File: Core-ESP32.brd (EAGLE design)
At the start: 149.8 x 80.5 mm, 58 parts, among them J2 CONNECTOR-GROVE-4P-2.0-347013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, Q1 BSS138, Q10 BSS138, Q11 BSS138, Q12 BSS138, Q13 BSS138, Q2 BSS138, Q3 BSS138, Q4 BSS138, Q5 BSS138, Q6 BSS138, Q7 BSS138, Q8 BSS138, Q9 BSS138

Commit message: 2.0
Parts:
- removed C4: 10uF, SPCoast:0805-CAP
- removed ESP32: ESP32, SPCoast:ESP32-LOLIN-OLED
- removed JP3: (no value), SparkFun-Connectors:1X06_LOCK
- added I2CLED32, I2CLED64: (no value), SPCoast:1X04_LOCK
- added IO-A, IO-B, IO-C: (no value), SparkFun-Connectors:1X06_LOCK
- added J5: (no value), SPCoast:RJ25-INVERTED
- added R27: 10k, SPCoast:0805-RES
- added U$1: ESP32-GEEKCREITDOITV1, SPCoast:ESP32-GEEKCREIT
- C2: value 150uF -> 1.0uF; device SPCoast:0810-CAP -> SPCoast:0805-CAP
- C3: value 1.0uF -> 10uF
- J1: device SPCoast:DCJ0202 -> SPCoast:RJ25-INVERTED
- J2: value CONNECTOR-GROVE-4P-2.0-3470130P1 -> (none); device SPCoast:4P-2.0 -> SPCoast:DCJ0202
- J3: value (none) -> CONNECTOR-GROVE-4P-2.0-3470130P1; device SPCoast:RJ25-INVERTED -> SPCoast:4P-2.0
- JP1: value 5v I2C Power -> LED
- JP2: value (none) -> 5v I2C Power; device SparkFun-Connectors:1X06_LOCK -> SparkFun-Connectors:1X02_LOCK
- R1: value 10k -> 220R
- VR5.0: value 5v -> 78M05B
- moved J2 127.0 mm to (17.8, 11.4), turned to 0 degrees
- moved JP2 112.2 mm to (143.5, 29.2), turned to 180 degrees
- moved J3 106.0 mm to (142.2, 36.8), turned to 90 degrees
- moved JP1 71.2 mm to (85.1, 69.8)
- moved R1 59.5 mm to (85.1, 64.8), turned to 270 degrees
- moved R2 45.7 mm to (41.9, 35.6), turned to 180 degrees
- moved R15 44.6 mm to (41.9, 43.2)
- moved Q1 43.1 mm to (102.9, 38.7), turned to 0 degrees
- moved Q2 41.0 mm to (41.9, 39.4), turned to 0 degrees
- moved R4 34.6 mm to (52.1, 35.6), turned to 180 degrees
- moved J1 31.6 mm to (40.6, 9.78)
- moved R3 31.4 mm to (47.0, 35.6), turned to 180 degrees
- moved VR5.0 22.2 mm to (15.2, 41.9)
- moved OSHW1 22.2 mm to (15.2, 52.1)
- moved R13 21.9 mm to (97.8, 35.6)
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- renumbered LED1 to MATRIX1, LED2 to MATRIX2
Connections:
- removed net D15H: J3.3, JP2.3, Q4.3, R17.1
- removed net D26H: J4.5, JP3.5, Q10.3, R23.1
- removed net D36: ESP32.GPIO36, Q8.2, R10.1
- removed net D36H: J4.3, JP3.3, Q8.3, R21.1
- removed net RXH: J3.4, JP2.4, Q5.3, R18.1
- removed net TXH: J3.5, JP2.5, Q6.3, R19.1
- new net D18: Q6.2, R6.1, U$1.IO18
- new net D18H: IO-C.2, J5.2, Q6.3, R19.1
- new net D19: Q7.2, R7.1, U$1.IO19
- new net D19H: IO-C.3, J5.3, Q7.3, R20.1
- new net D23: Q10.2, R10.1, U$1.IO23
- new net D23H: IO-C.4, J5.4, Q10.3, R23.1
- new net D27: U$1.IO27
- new net D32: U$1.IO32
- new net D33: U$1.IO33
- new net D4: Q4.2, R4.1, U$1.IO4
- new net D4H: IO-B.4, J4.4, Q4.3, R17.1
- new net D5: Q5.2, R5.1, U$1.IO5
- new net D5H: IO-B.5, J4.5, Q5.3, R18.1
- new net N$1: JP1.1, R1.1
- new net RX2: IO-A.5, J1.5, U$1.RX2
- new net TX2: IO-A.4, J1.4, U$1.TX2
- net +3V3: now also I2CLED32.3, I2CLED64.3, IO-A.1, J1.1, R2.2, R4.2, U$1.3V3; no longer ESP32.+3V3@0, ESP32.+3V3@1, R15.2
- net +9V: now also C2.1, J2.1, J3.3, J3.4; no longer C2.+, C3.1, J1.1, J2.3, J2.4
- net D0: now also Q2.2, R2.1, U$1.IO0; no longer ESP32.GPIO0, Q3.2, R5.1
- net D0H: now also IO-B.2, J4.2, Q2.3, R15.1; no longer J3.2, JP2.2, Q3.3, R16.1
- net D12: now also Q13.2, R13.1, U$1.IO12; no longer ESP32.GPIO12, Q12.2, R14.1
- net D12H: now also Q13.3, R26.1; no longer Q12.3, R25.1
- net D13: now also Q1.2, R14.1, U$1.IO13; no longer ESP32.GPIO13, Q13.2, R15.1
- net D13H: now also Q1.3, R27.1; no longer Q13.3, R26.1
- net D14: now also Q12.2, R12.1, U$1.IO14; no longer ESP32.GPIO14, Q11.2, R13.1
- net D14H: now also Q12.3, R25.1; no longer Q11.3, R24.1
- net D15: now also JP1.2, U$1.IO15; no longer ESP32.GPIO15, Q4.2, R6.1
- net D2: now also Q3.2, R3.1, U$1.IO2; no longer ESP32.GPIO2, Q7.2, R9.1
- net D25: now also Q11.2, U$1.IO25; no longer ESP32.GPIO25, Q9.2
- net D25H: now also IO-C.5, J5.5, Q11.3, R24.1; no longer J4.4, JP3.4, Q9.3, R22.1
- net D26: now also U$1.IO26; no longer ESP32.GPIO26, Q10.2, R12.1
- net D2H: now also IO-B.3, J4.3, Q3.3, R16.1; no longer J4.2, JP3.2, Q7.3, R20.1
- net GND: now also C2.2, I2CLED32.4, I2CLED64.4, IO-A.6, IO-B.6, IO-C.6, J1.6, J2.3, J3.1, J3.2, J5.6, U$1.GND; no longer C2.-, C4.2, ESP32.GND@0, ESP32.GND@1, ESP32.GND@2, J1.2, J1.3, J2.1, J3.6, JP2.6, JP3.6
- net N$44: now also JP2.1; no longer JP1.1
- net RX: now also IO-A.3, J1.3, U$1.RX1; no longer ESP32.RXD0, Q5.2, R7.1
- net SCL: now also I2CLED32.2, I2CLED64.2, Q9.2, R9.1, U$1.SCL; no longer ESP32.SCL, Q2.2, R3.1
- net SCLH: now also Q9.3, R22.1; no longer Q2.3, R4.1
- net SDA: now also I2CLED32.1, I2CLED64.1, Q8.2, R8.1, U$1.SDA; no longer ESP32.SDA, Q1.2, R1.1
- net SDAH: now also Q8.3, R21.1; no longer Q1.3, R2.1
- net TX: now also IO-A.2, J1.2, U$1.TX1; no longer ESP32.TXD0, Q6.2, R8.1
- net VCCIO: now also C3.1, IO-B.1, IO-C.1, J5.1, JP2.2, R15.2, R27.2, U$1.5V; no longer C4.1, ESP32.+5V@0, ESP32.+5V@1, J3.1, JP1.2, JP2.1, JP3.1, R2.2, R4.2
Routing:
- net D15: track 24.3 -> 129.2 mm
- net D26: track 73.3 -> 0.00 mm, vias 2 -> 0
- net D36: track 69.3 -> 0.00 mm, vias 2 -> 0
- net +9V: track 259.6 -> 212.8 mm
- net D23H: track 0.00 -> 45.5 mm
- net D2: track 56.1 -> 16.2 mm, vias 2 -> 0
- net D5H: track 0.00 -> 37.1 mm
- net D4H: track 0.00 -> 35.1 mm
- net D25: track 71.8 -> 39.6 mm, vias 2 -> 1
- net TX2: track 0.00 -> 32.0 mm
- net RX2: track 0.00 -> 31.3 mm
- net D19H: track 0.00 -> 30.5 mm
- net D18H: track 0.00 -> 30.4 mm
- net VCCIO: track 365.5 -> 338.4 mm
- net D26H: track 26.2 -> 0.00 mm
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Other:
- board text added: "+"
- board text added: "-"
- board text added: "2018.05"
- board text added: "3v3"
- board text added: "3v3 I/O"
- board text added: "78M05"
- board text added: "D15 LED"
- board text added: "D18"
- board text added: "D19"
- board text added: "D23"
- board text added: "D4"
- board text added: "D5"
- board text added: "For use with Geekcreit ESP32 (dual 18-pin version)"
- board text added: "Geekcreit ESP32"
- board text added: "I2C OLED SSD 1306 128x32 -or- 128x64"
- board text added: "RX1"
- board text added: "RX2"
- board text added: "TX1"
- board text added: "TX2"
- board text added: "v2.0"
- board text removed: "2018.02"
- board text removed: "D15"
- board text removed: "D26"
- board text removed: "D36"
- board text removed: "For use with WeMOS Lolin ESP32 - OLED"
- board text removed: "RX"
- board text removed: "TX"
- board text removed: "WeMOS Lolin ESP32 - OLED"
- board text removed: "v1.0"

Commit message: 2.1
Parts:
- removed JP1: LED, SparkFun-Connectors:1X02_LOCK
- removed JP2: 5v I2C Power, SparkFun-Connectors:1X02_LOCK
- removed MATRIX1, MATRIX2: LEDMATRIX, SPCoast:LEDMATRIX
- removed R1: 220R, SPCoast:0805-RES
- added I2CLED1: (no value), SPCoast:1X04_LOCK
- added J6: (no value), SPCoast:RJ25-INVERTED
- added Q14: BSS138, SPCoast:SOT23
- added R28, R29: 10k, SPCoast:0805-RES
- BOARD: device SPCoast:BOARD-DINRAIL-3.17INX15CM -> SPCoast:BOARD-DINRAIL-3.17IN-NOHOLES
- moved J3 54.3 mm to (88.9, 26.7)
- moved I2C 53.6 mm to (88.9, 17.8)
- moved Q4 24.1 mm to (27.9, 39.4)
- moved R17 24.1 mm to (27.9, 43.2)
- moved R4 24.1 mm to (27.9, 35.6)
- moved Q5 24.1 mm to (33.0, 39.4)
- moved R18 24.1 mm to (33.0, 43.2)
- moved R5 24.1 mm to (33.0, 35.6)
- moved Q1 14.0 mm to (88.9, 39.5)
- moved Q13 14.0 mm to (83.8, 39.4)
- moved R13 14.0 mm to (83.8, 35.6)
- moved R26 14.0 mm to (83.8, 43.2)
- moved Q10 14.0 mm to (68.6, 39.4)
- moved Q11 14.0 mm to (73.7, 39.4)
- moved Q12 14.0 mm to (78.7, 39.4)
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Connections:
- removed net D0H: IO-B.2, J4.2, Q2.3, R15.1
- removed net D12H: MATRIX2.CS@1, Q13.3, R26.1
- removed net D2H: IO-B.3, J4.3, Q3.3, R16.1
- removed net N$1: JP1.1, R1.1
- removed net N$10: MATRIX1.CLK@1, MATRIX2.CLK@2
- removed net N$3: MATRIX1.DI, MATRIX2.DO
- removed net N$44: I2C.V+, I2C.V+@1, JP2.1
- removed net N$9: MATRIX1.CS@1, MATRIX2.CS@2
- new net D26H: J6.2, Q14.3, R29.1
- new net D27H: J6.4, Q13.3, R26.1
- new net D32H: IO-B.4, J4.4, Q2.3, R15.1
- new net D33H: IO-B.5, J4.5, Q3.3, R16.1
- net +3V3: now also I2CLED1.3, Q14.1, R28.2; no longer R1.2
- net D0: no longer Q2.2, R2.1
- net D12: no longer Q13.2, R13.1
- net D13H: now also J6.5; no longer MATRIX2.CLK@1
- net D14H: now also J6.3; no longer MATRIX2.DI
- net D15: no longer JP1.2
- net D2: no longer Q3.2, R3.1
- net D26: now also Q14.2, R28.1
- net D27: now also Q13.2, R13.1
- net D32: now also Q2.2, R2.1
- net D33: now also Q3.2, R3.1
- net D4H: now also IO-B.2, J4.2; no longer IO-B.4, J4.4
- net D5H: now also IO-B.3, J4.3; no longer IO-B.5, J4.5
- net GND: now also I2CLED1.4, J6.6; no longer MATRIX1.G@1, MATRIX1.G@2, MATRIX2.G@1, MATRIX2.G@2
- net SCL: now also I2CLED1.2
- net SDA: now also I2CLED1.1
- net VCCIO: now also I2C.V+, I2C.V+@1, J6.1, R29.2; no longer JP2.2, MATRIX1.V+@1, MATRIX1.V+@2, MATRIX2.V+@1, MATRIX2.V+@2
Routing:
- net D15: track 129.2 -> 0.00 mm, vias 2 -> 0
- net VCCIO: track 338.4 -> 249.5 mm, vias 13 -> 15
- net D26: track 0.00 -> 67.9 mm, vias 0 -> 2
- net N$10: track 64.0 -> 0.00 mm
- net N$3: track 63.7 -> 0.00 mm
- net N$9: track 63.4 -> 0.00 mm
- net D12: track 61.4 -> 0.00 mm, vias 1 -> 0
- net +9V: track 212.8 -> 156.9 mm
- net D27: track 0.00 -> 50.9 mm, vias 0 -> 1
- net D26H: track 0.00 -> 45.0 mm, vias 0 -> 2
- net D32: track 0.00 -> 41.1 mm, vias 0 -> 1
- net +3V3: track 238.3 -> 200.1 mm
- net SDAH: track 103.8 -> 69.5 mm
- net SCLH: track 93.3 -> 59.0 mm
- net D33: track 0.00 -> 32.6 mm, vias 0 -> 1
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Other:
- board size 149.8 x 80.5 mm -> 106 x 100 mm
- board text added: "2018.07"
- board text added: "CS"
- board text added: "Clk"
- board text added: "D13"
- board text added: "D14"
- board text added: "D26"
- board text added: "D27"
- board text added: "D32"
- board text added: "D33"
- board text added: "Data"
- board text added: "Geekcreit ESP32 WROOM"
- board text added: "IO1"
- board text added: "v2.1"
- board text removed: "+"
- board text removed: "-"
- board text removed: "2018.05"
- board text removed: "CS D12"
- board text removed: "Clock D13"
- board text removed: "D0"
- board text removed: "D15 LED"
- board text removed: "D2"
- board text removed: "Data D14"
- board text removed: "Geekcreit ESP32"
- board text removed: "v2.0"

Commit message: 2.2
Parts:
- C2, C3: device SPCoast:0805-CAP -> SPCoast:0603-CAP
- R10, R11, R12, R13, R14, R15, R16, R17, R18, R19, R2, R20, R21, R22, R23, R24, R25, R26, R27, R28, R29, R3, R4, R5, R6, R7, R8, R9: device SPCoast:0805-RES -> SPCoast:0603-RES
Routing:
- net +3V3: track 200.1 -> 200.8 mm
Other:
- board text added: "0603 version"
- board text added: "v2.2"
- board text removed: "v2.1"

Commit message: 2.3
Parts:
- added MT1, MT2, MT3, MT4: MOUNTINGHOLE, SPCoast:MOUNTINGHOLE
- moved LABEL1 15.2 mm to (3.81, 25.4)
- moved I2CLED64 10.5 mm to (66.0, 27.9)
- moved J2 10.2 mm to (16.5, 24.1)
- moved Q10 10.2 mm to (68.6, 49.5)
- moved Q11 10.2 mm to (73.7, 49.5)
- moved Q12 10.2 mm to (78.7, 49.5)
- moved Q13 10.2 mm to (83.8, 49.5)
- moved Q14 10.2 mm to (94.0, 49.5)
- moved Q2 10.2 mm to (38.1, 49.5)
- moved Q3 10.2 mm to (43.2, 49.5)
- moved Q4 10.2 mm to (27.9, 49.5)
- moved Q5 10.2 mm to (33.0, 49.5)
- moved Q6 10.2 mm to (48.3, 49.5)
- moved Q7 10.2 mm to (53.3, 49.5)
- moved Q8 10.2 mm to (58.4, 49.5)
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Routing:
- net +9V: track 157.0 -> 146.6 mm
- net SDA: track 58.6 -> 68.9 mm
- net SCL: track 53.3 -> 61.6 mm, vias 0 -> 1
- net SCLH: track 59.0 -> 55.2 mm
- net VCCIO: track 249.7 -> 253.3 mm
- net +3V3: track 200.8 -> 197.2 mm
- net SDAH: track 69.5 -> 66.4 mm
- net D5: track 32.9 -> 29.9 mm
- net D26: track 67.9 -> 68.7 mm
- net D4: track 29.4 -> 28.6 mm
- net D26H: track 45.0 -> 45.7 mm
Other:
- board text added: "0603"
- board text added: "128x32 -or- 128x64"
- board text added: "2018.12"
- board text added: "Changes: Moved OLED connector to not cover WROOM radio module Added mounting holes fixed bottom silkscreen"
- board text added: "Field Unit"
- board text added: "I/O"
- board text added: "I2C OLED SSD 1306"
- board text added: "IO4"
- board text added: "IO4 breakout, I2C master and LCD display"
- board text added: "IO4 breakout, I2C master, LCD display"
- board text added: "v2.3"
- board text removed: "0603 version"
- board text removed: "2018.07"
- board text removed: "Field Unit Processor"
- board text removed: "I2C OLED SSD 1306 128x32 -or- 128x64"
- board text removed: "IO1"
- board text removed: "IO4 breakout, I2C master and Codeline Matrix"
- board text removed: "v2.2"

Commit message: 2.4
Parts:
- added IO-D: (no value), SparkFun-Connectors:1X06_LOCK
- moved IO-B 1.27 mm to (24.5, 69.8)
- moved IO-C 1.27 mm to (49.3, 69.8)
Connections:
- net D13H: now also IO-D.5
- net D14H: now also IO-D.3
- net D26H: now also IO-D.2
- net D27H: now also IO-D.4
- net GND: now also IO-D.6
- net VCCIO: now also IO-D.1
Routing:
- net GND: track 0.00 -> 18.8 mm
- net +9V: track 146.6 -> 150.3 mm
- net D26H: track 45.7 -> 47.5 mm
- net VCCIO: track 253.3 -> 254.9 mm
- net D14H: track 27.3 -> 27.9 mm
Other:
- board text added: "2019.03"
- board text added: "Changes: Convert old CodeLine connector to IO4 "D" Beefed up VIN traces"
- board text added: "v2.4"
- board text removed: "2018.12"
- board text removed: "CS"
- board text removed: "Changes: Moved OLED connector to not cover WROOM radio module Added mounting holes fixed bottom silkscreen"
- board text removed: "Clk"
- board text removed: "Codeline"
- board text removed: "Data"
- board text removed: "I/O"
- board text removed: "v2.3"

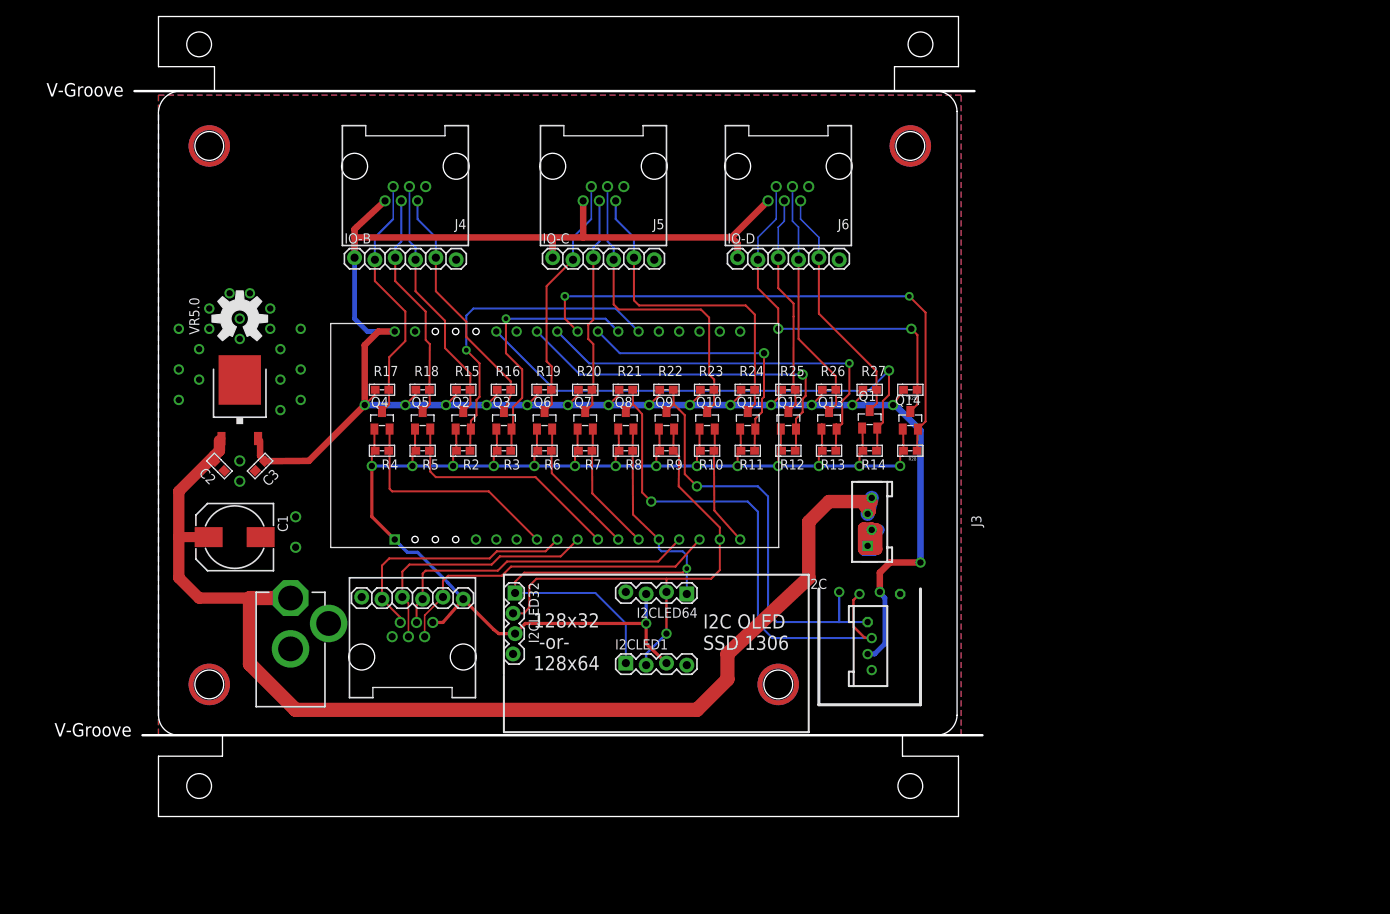
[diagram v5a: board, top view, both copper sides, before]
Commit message: switched to 30-pin dev board from larger Geekreit one
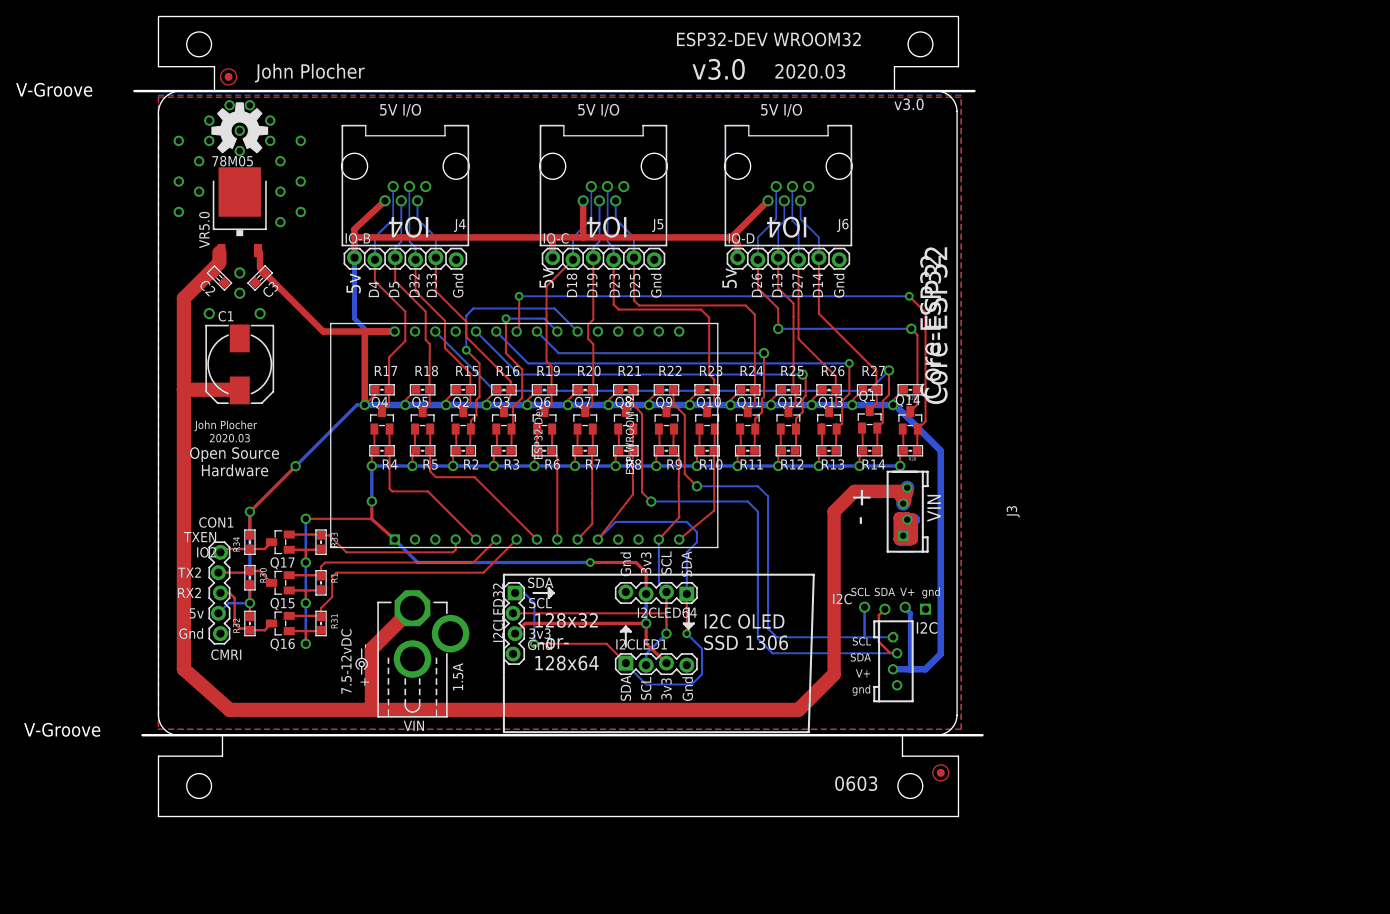
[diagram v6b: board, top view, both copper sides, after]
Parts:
- removed IO-A: (no value), SparkFun-Connectors:1X06_LOCK
- removed J1: (no value), SPCoast:RJ25-INVERTED
- removed MT1, MT2, MT3, MT4: MOUNTINGHOLE, SPCoast:MOUNTINGHOLE
- added CON1: (no value), SPCoast:1X05_LOCK
- added FID1, FID2: FIDUCIAL, SPCoast:FIDUCIAL_1MM
- added Q15, Q16, Q17: BSS138, SPCoast:SOT23
- added R1, R30, R31, R32, R33, R34: 10k, SPCoast:0603-RES
- BOARD: device SPCoast:BOARD-DINRAIL-3.17IN-NOHOLES -> SPCoast:BOARD-DINRAIL-3.17IN-IOB
- IO-B, IO-C, IO-D: device SparkFun-Connectors:1X06_LOCK -> SPCoast:1X06_LOCK
- LABEL1: device SPCoast-minimal:POWER_USAGE -> SPCoast:PWR_LABEL
- U$1: value ESP32-GEEKCREITDOITV1 -> ESP32/DEV; device SPCoast:ESP32-GEEKCREIT -> SPCoast:ESP32-DEV
- moved C2 23.5 mm to (7.62, 67.3)
- moved C3 23.5 mm to (12.7, 67.3)
- moved OSHW1 23.5 mm to (10.2, 85.7)
- moved VR5.0 23.5 mm to (10.2, 75.6)
- moved LABEL1 22.5 mm to (25.4, 19.1)
- moved C1 21.6 mm to (10.2, 56.5), turned to 270 degrees
- moved J2 15.3 mm to (31.8, 22.9)
- moved J3 4.62 mm to (93.3, 38.1)
- moved I2C 3.70 mm to (92.1, 26.0)
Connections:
- removed net D0: U$1.IO0
- new net D2H: CON1.1, Q17.3, R34.1
- new net RX2H: CON1.2, Q15.3, R30.1
- new net TX2H: CON1.3, Q16.3, R32.1
- net +3V3: now also Q15.1, Q16.1, Q17.1, R1.2, R31.2, R33.2; no longer IO-A.1, J1.1
- net D2: now also Q17.2, R33.1
- net GND: now also CON1.5, U$1.GND@1; no longer IO-A.6, J1.6
- net RX: no longer IO-A.3, J1.3
- net RX2: now also Q15.2, R1.1; no longer IO-A.5, J1.5
- net TX: no longer IO-A.2, J1.2
- net TX2: now also Q16.2, R31.1; no longer IO-A.4, J1.4
- net VCCIO: now also CON1.4, R30.2, R32.2, R34.2
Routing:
- net VCCIO: track 254.9 -> 312.7 mm, vias 15 -> 17
- net +3V3: track 197.2 -> 249.1 mm, vias 15 -> 21
- net +9V: track 150.3 -> 199.0 mm
- net TX: track 42.3 -> 0.00 mm
- net RX: track 40.3 -> 0.00 mm
- net D2: track 0.00 -> 23.1 mm
- net SDA: track 68.9 -> 79.9 mm, vias 1 -> 2
- net TX2H: track 0.00 -> 10.5 mm
- net SCL: track 61.6 -> 51.5 mm
- net D4: track 28.6 -> 21.0 mm
- net D14: track 45.7 -> 53.3 mm
- net D13: track 63.9 -> 71.5 mm
- net D33: track 32.7 -> 25.0 mm
- net D5: track 29.9 -> 22.3 mm
- net D32: track 41.1 -> 33.5 mm
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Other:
- board text added: "2020.03"
- board text added: ">DRAWING_NAME"
- board text added: "CMRI"
- board text added: "ESP32-DEV WROOM32"
- board text added: "TXEN IO2"
- board text added: "v3.0"
- board text removed: "2019.03"
- board text removed: "3v3 I/O"
- board text removed: "Changes: Convert old CodeLine connector to IO4 "D" Beefed up VIN traces"
- board text removed: "Field Unit"
- board text removed: "Geekcreit ESP32 WROOM"
- board text removed: "RX1"
- board text removed: "TX1"
- board text removed: "v2.4"
